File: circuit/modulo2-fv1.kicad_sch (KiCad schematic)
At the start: 61 parts, among them J1 CONN_01X04, J2 CONN_01X04, J3 CONN_01X02, J4 HOLE, J5 HOLE, SW1 ROTENC_BOURNS_PEL12D, U1 NE5532, U10 TLE2426, U3 FV-1, U4 AVR-ISP6, U5 LM1117 3V3, U6 ATmega328p, U7 DBG_UART, U8 74164, Y1 16MHz

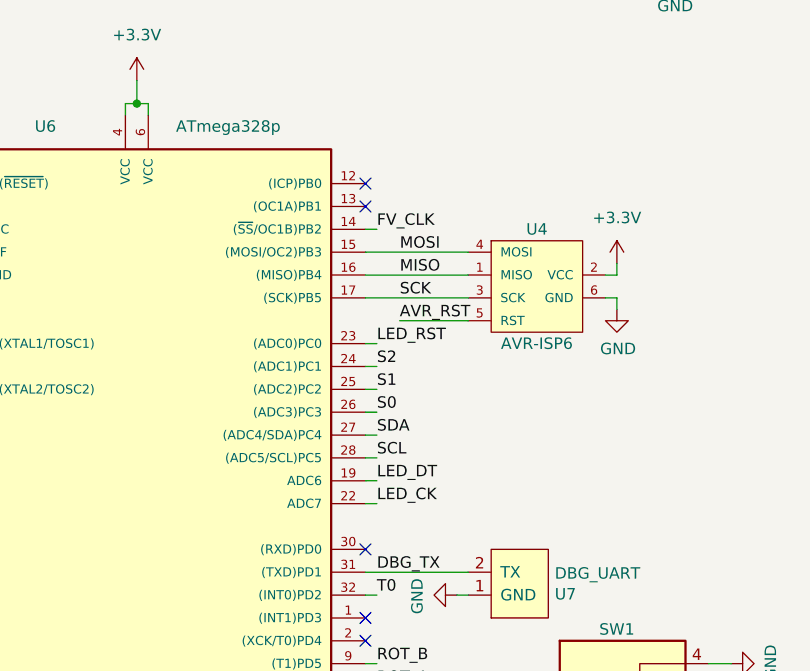
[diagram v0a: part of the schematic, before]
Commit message: FV-1 firmware reworked for the new board; FV-1 PCB needs rework to correct errors
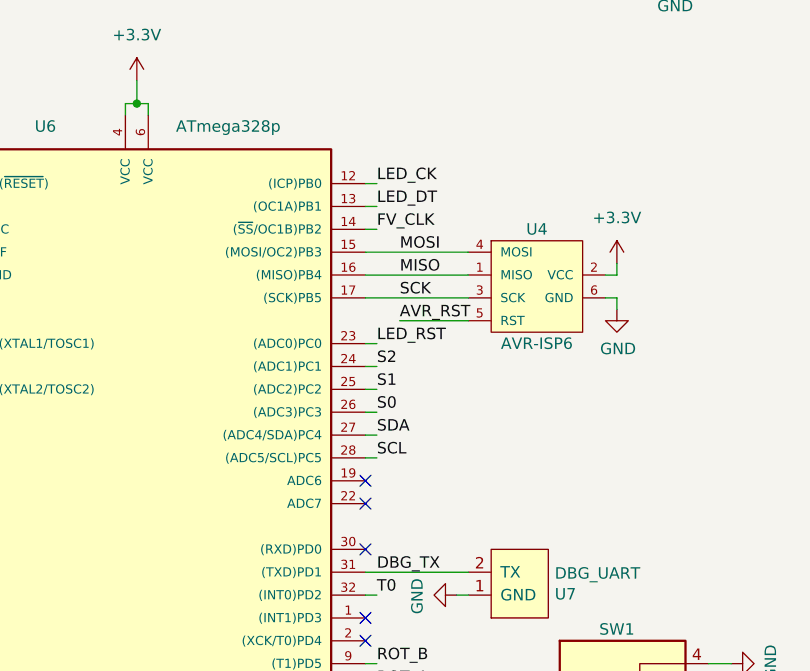
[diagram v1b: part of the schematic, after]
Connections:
- net LED_CK: now also U6.12 ((ICP)PB0); no longer U6.22 (ADC7)
- net LED_DT: now also U6.13 ((OC1A)PB1); no longer U6.19 (ADC6)
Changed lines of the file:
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@@
   (no_connect (at 232.41 132.08))
   (no_connect (at 232.41 129.54))
-  (no_connect (at 232.41 83.82))
-  (no_connect (at 232.41 81.28))
+  (no_connect (at 232.41 114.3))
+  (no_connect (at 232.41 116.84))
   (no_connect (at 162.56 190.5))
   (no_connect (at 232.41 121.92))
@@
     (stroke (width 0) (type default) (color 0 0 0 0))
   )
-  (wire (pts (xy 232.41 114.3) (xy 233.68 114.3))
-    (stroke (width 0) (type default) (color 0 0 0 0))
-  )
   (wire (pts (xy 125.73 50.8) (xy 125.73 52.07))
     (stroke (width 0) (type default) (color 0 0 0 0))
@@
     (stroke (width 0) (type default) (color 0 0 0 0))
   )
-  (wire (pts (xy 233.68 116.84) (xy 232.41 116.84))
-    (stroke (width 0) (type default) (color 0 0 0 0))
-  )
   (wire (pts (xy 207.01 72.39) (xy 208.28 72.39))
     (stroke (width 0) (type default) (color 0 0 0 0))
@@
     (stroke (width 0) (type default) (color 0 0 0 0))
   )
+  (wire (pts (xy 232.41 83.82) (xy 233.68 83.82))
+    (stroke (width 0) (type default) (color 0 0 0 0))
+  )
   (wire (pts (xy 250.825 27.94) (xy 257.81 27.94))
     (stroke (width 0) (type default) (color 0 0 0 0))
@@
     (stroke (width 0) (type default) (color 0 0 0 0))
   )
+  (wire (pts (xy 232.41 81.28) (xy 233.68 81.28))
+    (stroke (width 0) (type default) (color 0 0 0 0))
+  )
   (wire (pts (xy 241.3 48.26) (xy 250.825 48.26))
     (stroke (width 0) (type default) (color 0 0 0 0))
@@
     (effects (font (size 1.27 1.27)) (justify left bottom))
   )
-  (label "LED_CK" (at 233.68 116.84 0)
+  (label "LED_CK" (at 233.68 81.28 0)
     (effects (font (size 1.27 1.27)) (justify left bottom))
   )
@@
     (effects (font (size 1.27 1.27)) (justify left bottom))
   )
-  (label "LED_DT" (at 233.68 114.3 0)
-    (effects (font (size 1.27 1.27)) (justify left bottom))
-  )
+  (label "LED_DT" (at 233.68 83.82 0)
+    (effects (font (size 1.27 1.27)) (justify left bottom))
+  )

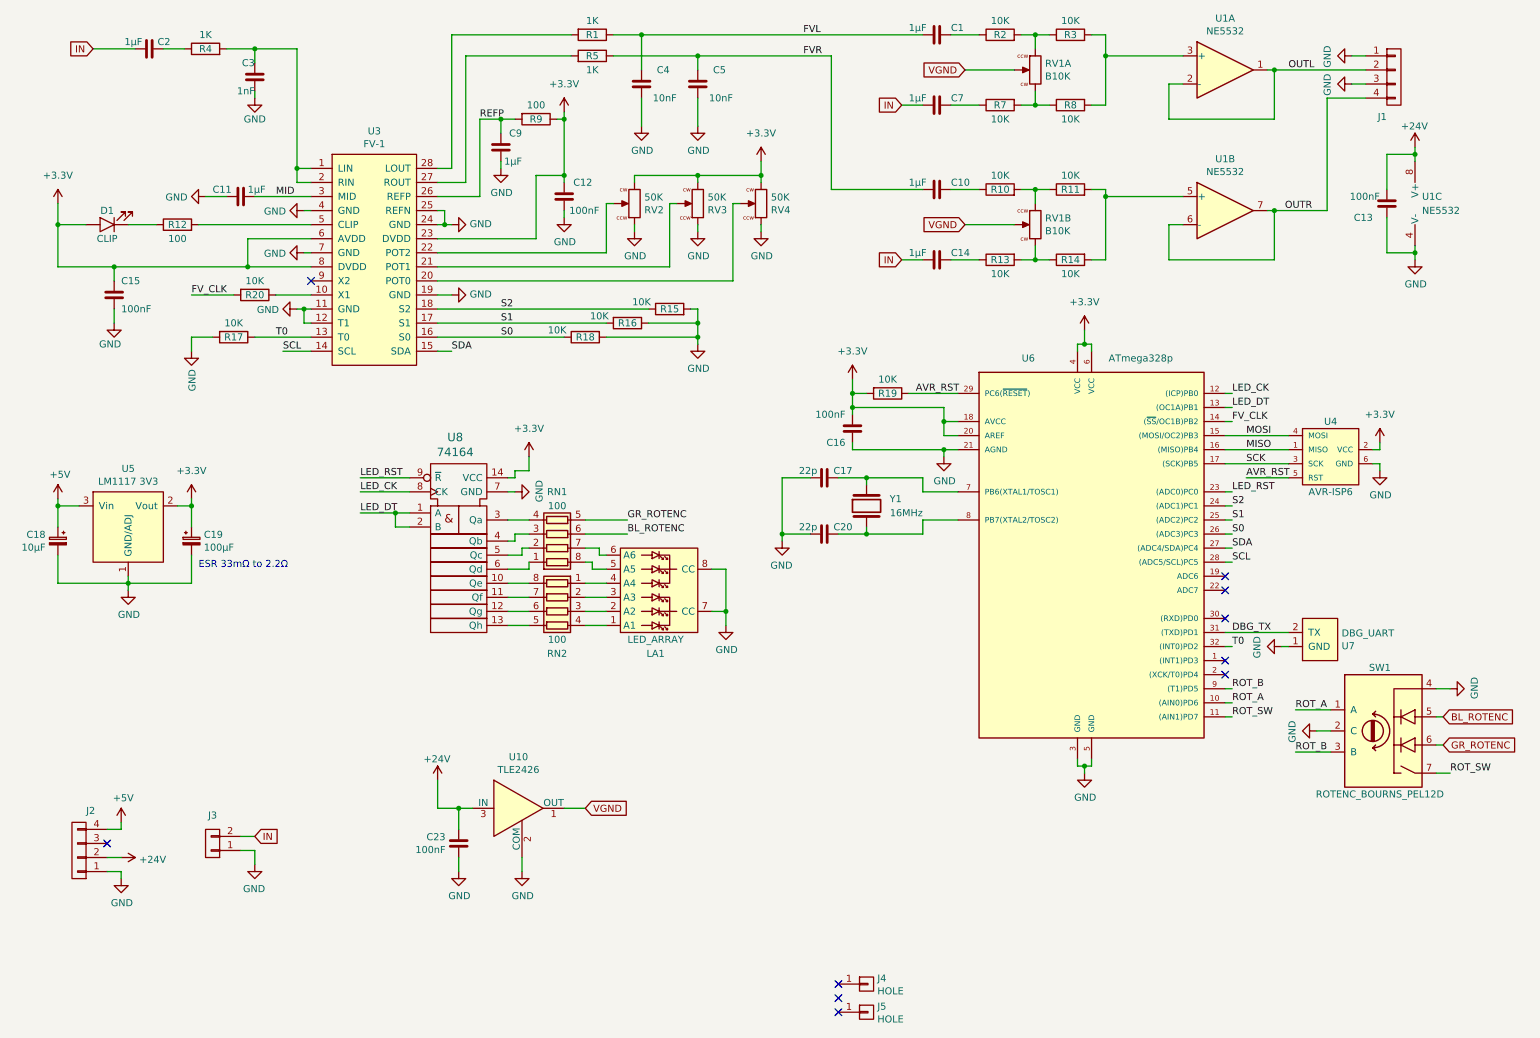
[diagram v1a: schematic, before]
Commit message: added report on createBanks.py; started PCB redesign
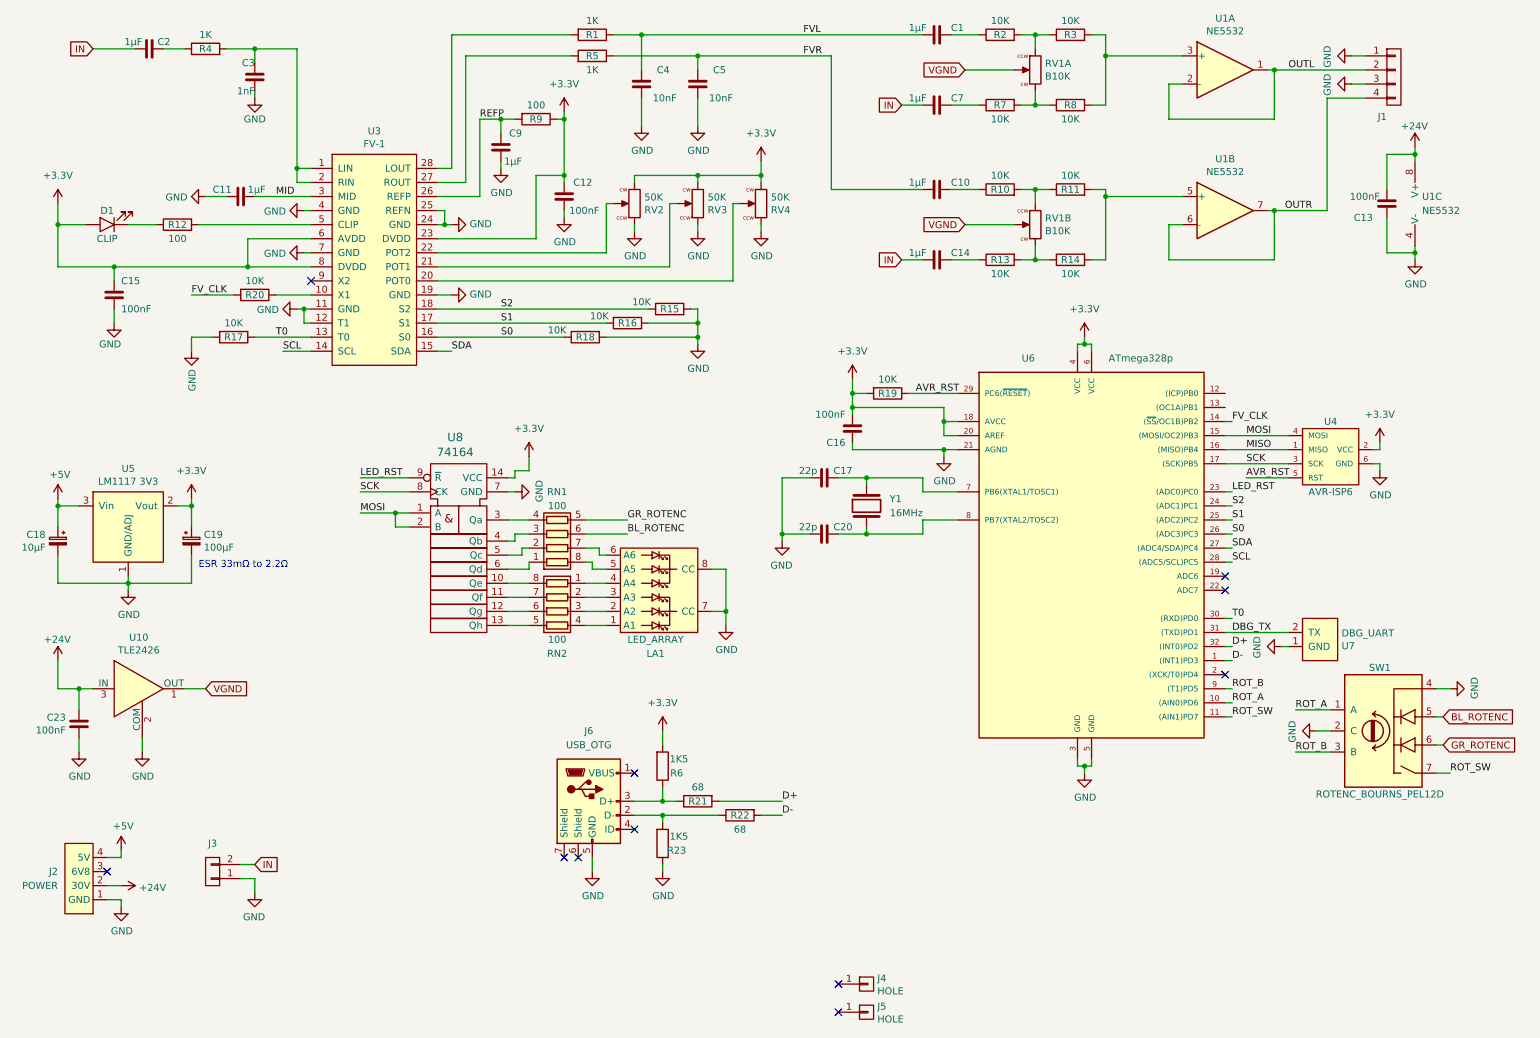
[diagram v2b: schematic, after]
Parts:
- removed J2: CONN_01X04, myAmp:PIN_1x04, symbol myAmp:CONN_01X04
- added J2: POWER, myAmp:POWER, symbol myAmp:POWER
- added J6: USB_OTG, myAmp:USB_OTG_THT, symbol myAmp:USB_OTG
- added R21, R22: 68, myAmp:R_10MM, symbol myAmp:R
- added R23, R6: 1K5, myAmp:R_10MM, symbol myAmp:R
- C1, C10, C14, C7: footprint myAmp:C_FILM_L7.2mm_W4.5mm_P5.00mm -> myAmp:C_FILM_L7.2mm_W5.0mm_P5.00mm
- C17, C20: footprint myAmp:C_2.5MM -> myAmp:C_5MM_1206
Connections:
- net +24V: now also J2.2 (30V)
- net +3V3: now also R6.2
- net +5V: now also J2.4 (5V)
- net GND: now also J2.1 (GND), J6.5 (GND), R23.1
- net MOSI: now also U8.1 (A), U8.2 (B)
- net SCK: now also U8.8 (CK)
- net T0: now also U6.30 ((RXD)PD0); no longer U6.32 ((INT0)PD2)
- net D-: now reaches U6.1 ((INT1)PD3)
- net D-: now also R22.2
- net LED_CK: no longer names the net of U6.12 ((ICP)PB0)
- net LED_CK: no longer U8.8 (CK)
- removed net LED_DT: U6.13 ((OC1A)PB1), U8.1 (A), U8.2 (B)
- new net: J6.3 (D+), R21.1, R6.1
- new net: J6.2 (D-), R22.1, R23.2
- new net D+: R21.2, U6.32 ((INT0)PD2)
- no-connect marks 10 -> 11
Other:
- moved on the sheet: C23, J3, U10

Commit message: routed pa27; routing fv-1
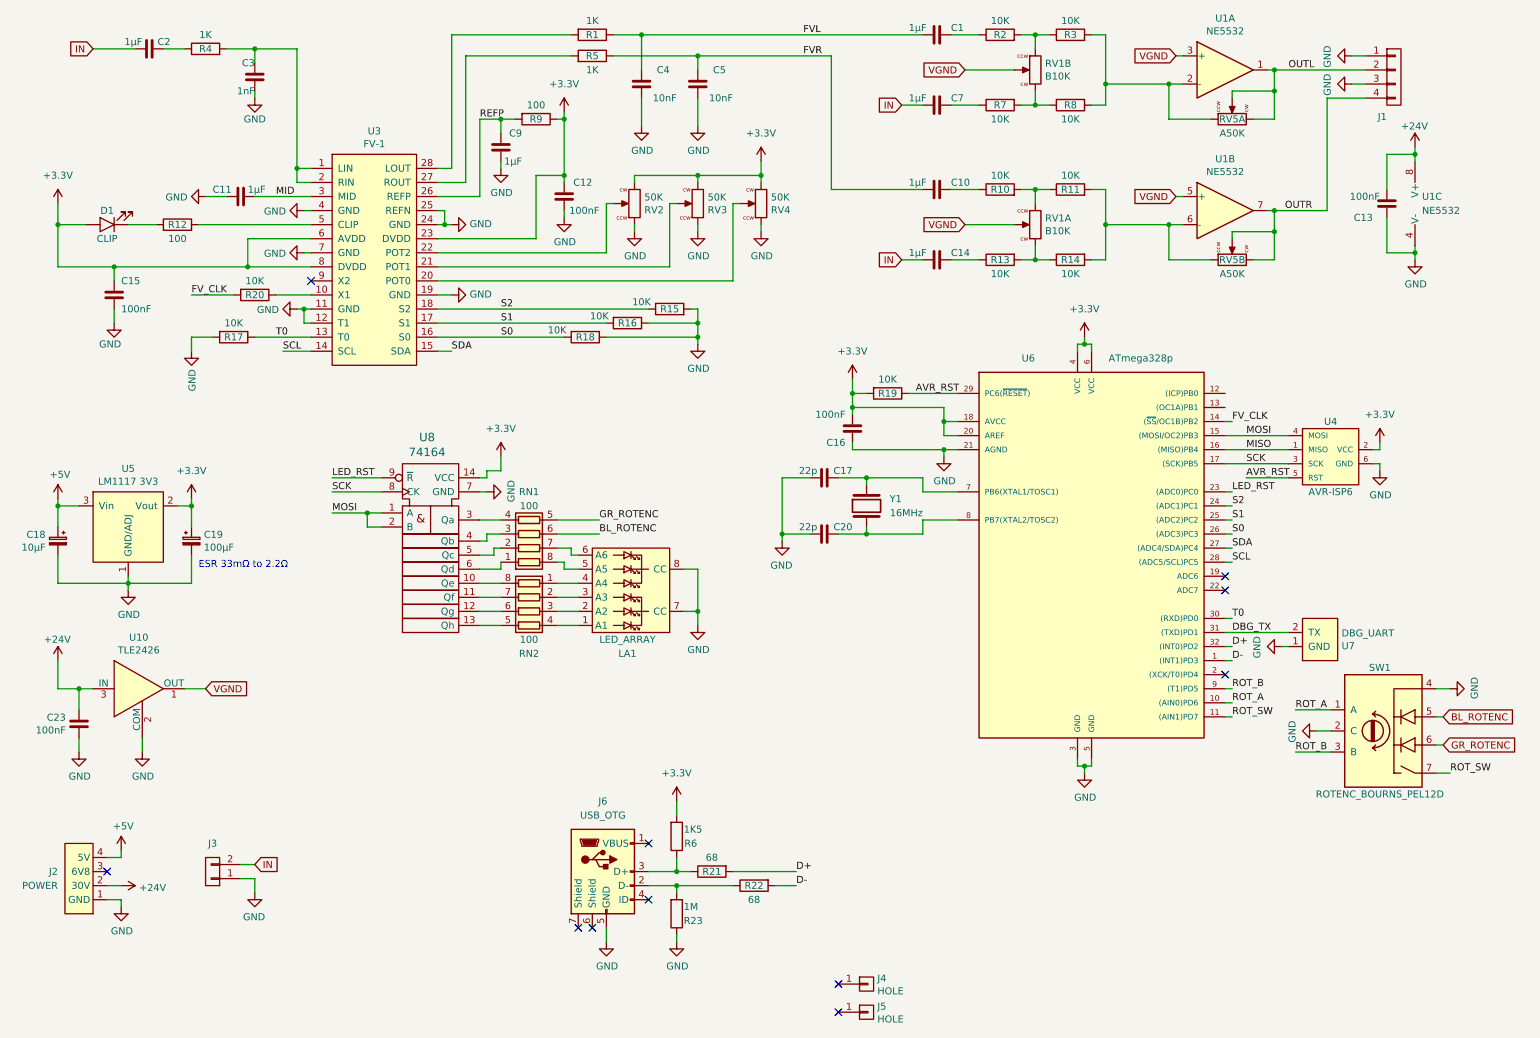
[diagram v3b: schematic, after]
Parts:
- added RV5: A50K, myAmp:BOURNS_PTD902_xx15K, symbol myAmp:R_POT_DBL
- C3, C4, C5: footprint myAmp:C_FILM_L7.2mm_W2.5mm_P5.00mm -> myAmp:C_1206
- R1, R10, R11, R13, R14, R2, R3, R5, R7, R8: footprint myAmp:R_10MM -> myAmp:R_1206
- R23: value 1K5 -> 1M
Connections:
- net OUTL: now also RV5.2, RV5.3; no longer U1.2 (-)
- net OUTR: now also RV5.5 (2), RV5.6 (3); no longer U1.6 (-)
- net VGND: now also U1.3 (+), U1.5 (+)
- net at R7.2, R8.1: now also RV1.6 (3); no longer RV1.3
- net at R3.2, R8.2: now also U1.2 (-), RV5.1; no longer U1.3 (+)
- net at R10.2, R11.1: now also RV1.1; no longer RV1.4 (1)
- net at R11.2, R14.2: now also U1.6 (-), RV5.4 (1); no longer U1.5 (+)
- net at R2.2, R3.1: now also RV1.4 (1); no longer RV1.1
- net at R13.2, R14.1: now also RV1.3; no longer RV1.6 (3)
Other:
- moved on the sheet: J6, LA1, R21, R22, R23, R6, RN1, RN2, RV1A, RV1B, U8
